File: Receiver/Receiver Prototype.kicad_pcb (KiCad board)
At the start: 4 copper layers, 145 x 50.8 mm, 96 parts, among them J1 Conn_01x02_Socket, J10 Conn_01x01, J11 Conn_Coaxial, J12 Conn_Coaxial, J13 Conn_Coaxial, J14 Conn_Coaxial, J15 Conn_01x01, J17 Conn_01x02, J18 Conn_01x02, J2 Conn_01x01, J20 Conn_01x01, J21 Conn_01x01, J22 Conn_01x01, J23 Conn_01x02, J24 Conn_01x02, J25 Conn_01x01, J26 Conn_01x03, J27 Conn_01x03, J28 Conn_01x02, J3 Conn_01x01, J4 Conn_Coaxial, J5 Conn_01x01, J6 Conn_01x02, J7 Conn_Coaxial, J8 Conn_Coaxial, J9 Conn_01x01, U1 OPA3692ID, U2 AD8692ARZ, U3 OPA692IDBVR, U4 LT3045EMSE-PBF, U5 AD607ARSZ, U6 LT3094EMSE-PBF

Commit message: DR2
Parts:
- J13, J14: footprint BNC 112404:CONN_112404_AMP -> Connector_Coaxial:BNC_Amphenol_B6252HB-NPP3G-50_Horizontal
- moved J25 8.11 mm to (187.2, 80.0)
- moved J8 6.03 mm to (179.7, 98.1)
- moved J14 5.50 mm to (196.5, 87.7), turned to 180 degrees
- moved J13 4.36 mm to (215.5, 87.7), turned to 180 degrees
- moved J7 3.50 mm to (165.2, 98.1)
- moved J15 1.58 mm to (206.8, 80.0)
- moved J2 1.50 mm to (224.2, 80.0)
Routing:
- net /PWR-: track 73.7 -> 63.1 mm
- net /PWR+: track 76.1 -> 69.1 mm
- net /I_Filter_In: track 29.3 -> 27.9 mm
- net GND: vias 10 -> 14

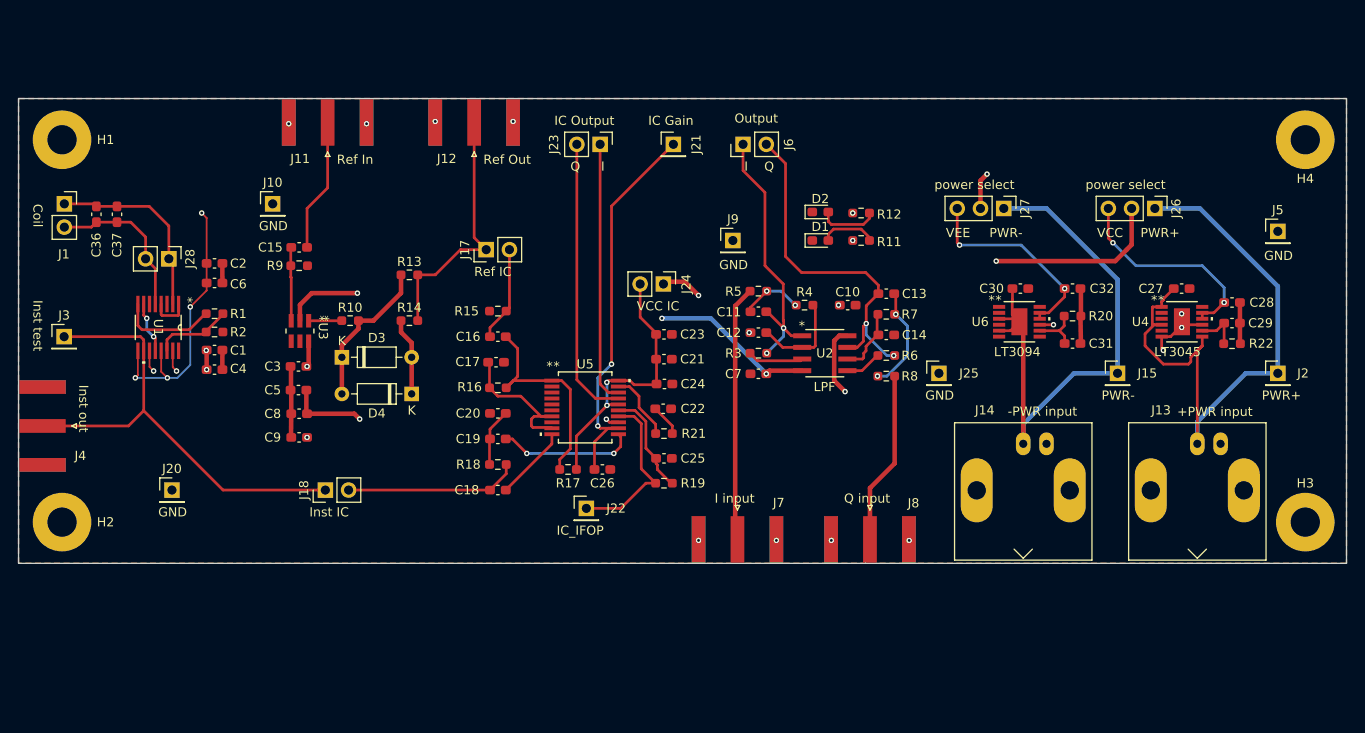
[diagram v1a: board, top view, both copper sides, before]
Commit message: Moved some components. Design not complete for the DR2
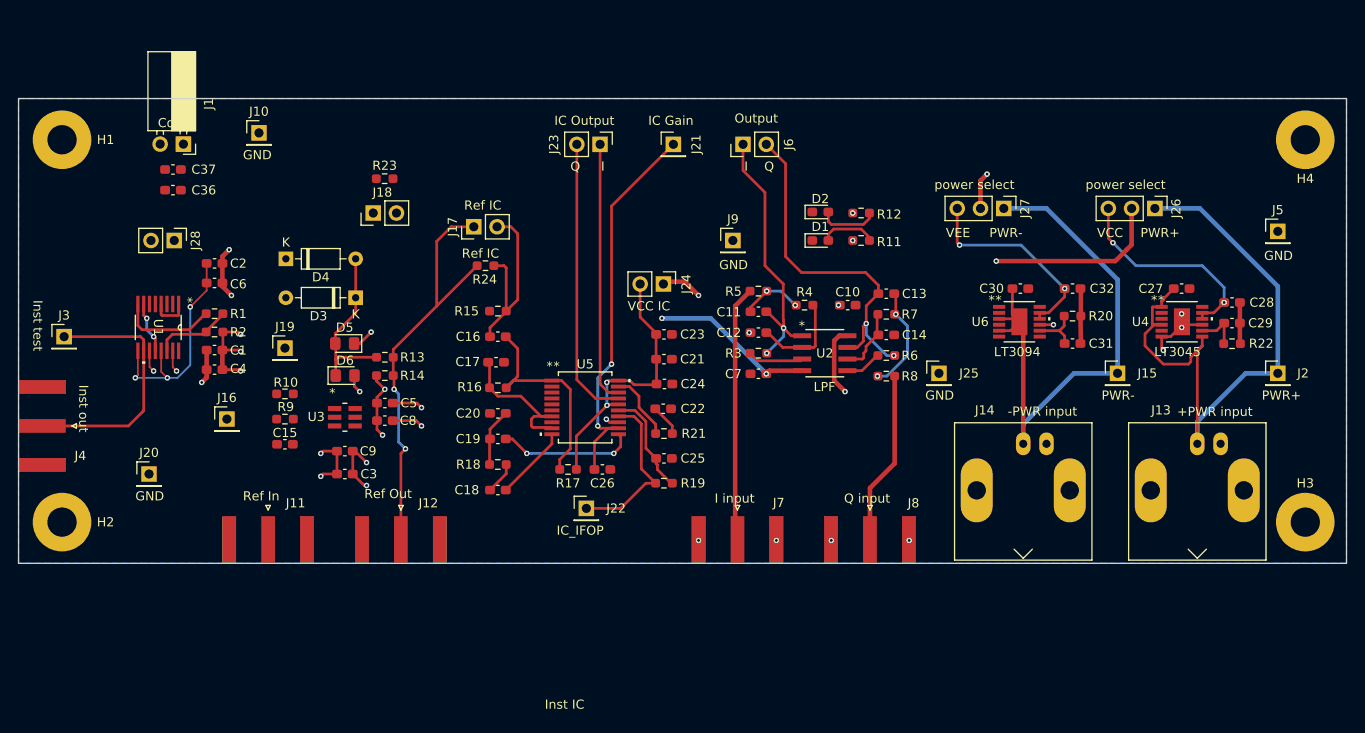
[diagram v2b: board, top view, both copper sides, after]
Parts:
- added D5: 1N4148, Diode_SMD:D_0805_2012Metric_Pad1.15x1.40mm_HandSolder, F.Cu at (122.4, 76.8)
- added D6: 1N4148, Diode_SMD:D_0805_2012Metric_Pad1.15x1.40mm_HandSolder, F.Cu at (122.4, 80.2)
- added J16: Conn_01x01, Connector_PinHeader_2.54mm:PinHeader_1x01_P2.54mm_Vertical, F.Cu at (109.5, 85.0)
- added J19: Conn_01x01, Connector_PinHeader_2.54mm:PinHeader_1x01_P2.54mm_Vertical, F.Cu at (115.8, 77.2)
- added R23: 0, Resistor_SMD:R_0603_1608Metric_Pad0.98x0.95mm_HandSolder, F.Cu at (126.7, 58.8)
- added R24: 0, Resistor_SMD:R_0603_1608Metric_Pad0.98x0.95mm_HandSolder, F.Cu at (137.7, 68.2)
- J1: footprint Connector_PinSocket_2.54mm:PinSocket_1x02_P2.54mm_Vertical -> Connector_PinSocket_2.54mm:PinSocket_1x02_P2.54mm_Horizontal
- moved J12 46.2 mm to (128.5, 98.1), turned to -90 degrees
- moved J11 46.0 mm to (114.0, 98.1), turned to -90 degrees
- moved J18 30.7 mm to (125.5, 62.5)
- moved C15 21.6 mm to (115.8, 87.8), turned to 0 degrees
- moved D4 20.2 mm to (115.9, 67.5), turned to 0 degrees
- moved R9 16.8 mm to (115.8, 85.0), turned to 180 degrees
- moved J1 14.5 mm to (104.8, 55.0), turned to -90 degrees
- moved C3 12.8 mm to (122.4, 91.0)
- moved R10 10.7 mm to (115.8, 82.2)
- moved U3 10.6 mm to (122.4, 84.8), turned to 0 degrees
- moved C5 9.54 mm to (126.8, 83.2)
- moved C8 9.39 mm to (126.8, 85.2)
- moved R13 9.39 mm to (126.8, 78.2)
- moved C36 8.77 mm to (103.6, 60.0), turned to 0 degrees
- moved J10 7.89 mm to (113.0, 53.8)
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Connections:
- net Net-(U3-IN+) renamed /Buff_In
- net Net-(U3-OUPUT) renamed /Buff_Out
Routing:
- net /Inst_Out: track 70.7 -> 31.8 mm
- net /Reference_Out: track 38.4 -> 67.5 mm, vias 0 -> 2
- net /INA: track 21.1 -> 0.00 mm
- net /INB: track 17.5 -> 0.00 mm
- net VEE: track 69.7 -> 53.5 mm, vias 10 -> 9
- net /Reference_In: track 14.6 -> 0.00 mm
- net GND: track 42.3 -> 55.9 mm, vias 14 -> 21
- net /Buff_In: track 8.06 -> 0.00 mm
- net VCC: track 41.6 -> 46.9 mm, vias 11 -> 10
- net /Buff_Out: track 3.62 -> 0.00 mm
- net Net-(D3-K): track 16.6 -> 18.3 mm
- removed copper zone on F.Cu, net GND

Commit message: Receiver ready for design review 2
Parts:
- moved J18 36.3 mm to (103.0, 91.0)
- moved R23 35.5 mm to (104.2, 86.2)
- moved J1 25.3 mm to (129.8, 51.4)
- moved C37 25.0 mm to (128.5, 55.4), turned to 180 degrees
- moved C36 24.9 mm to (128.5, 58.4), turned to 180 degrees
- moved J10 11.8 mm to (102.0, 58.1)
- moved J28 9.12 mm to (112.5, 62.8), turned to 180 degrees
- moved J20 3.75 mm to (97.2, 91.0)
- moved R24 1.84 mm to (139.1, 69.5)
- moved J17 1.78 mm to (137.7, 65.2)
- moved J16 1.77 mm to (110.8, 83.8)
- moved J19 1.76 mm to (116.8, 75.8)
- moved J15 1.75 mm to (205.0, 80.0)
- moved J25 1.75 mm to (189.0, 80.0)
- moved U3 1.75 mm to (122.4, 86.5)
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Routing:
- net /Inst_Out: track 31.8 -> 82.6 mm, vias 0 -> 2
- net /INA: track 0.00 -> 43.6 mm
- net /INB: track 0.00 -> 43.3 mm
- net GND: track 55.9 -> 39.1 mm, vias 21 -> 218
- net /Buff_Out: track 0.00 -> 15.9 mm
- net /Buff_In: track 0.00 -> 12.8 mm
- net /Reference_In: track 0.00 -> 10.8 mm
- net /Reference_Out: track 67.5 -> 58.8 mm
- net VEE: track 53.5 -> 62.2 mm, vias 9 -> 11
- net Net-(D3-K): track 18.3 -> 23.7 mm
- net /PWR+: track 69.1 -> 63.7 mm
- net /PWR-: track 63.1 -> 59.5 mm
- net Net-(C13-Pad2): track 11.5 -> 13.8 mm
- net Net-(U5-GREF): track 16.4 -> 15.2 mm
- net /I_Filter_Out: track 30.4 -> 31.3 mm
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- added copper zone on F.Cu, net GND
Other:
- outline, holes or cut-outs redrawn
- board text added: "Buff In"
- board text added: "Buff Out"
- board text added: "Coil test"

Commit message: Receiver minor fixes before DR2
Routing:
- net VEE: track 62.2 -> 52.6 mm, vias 11 -> 12
- net /IC_Gain: track 42.8 -> 45.5 mm
- net /VCC_IC: track 29.8 -> 31.9 mm
- net /IC_I: track 28.6 -> 30.2 mm
- net GND: track 39.1 -> 38.7 mm, vias 218 -> 224

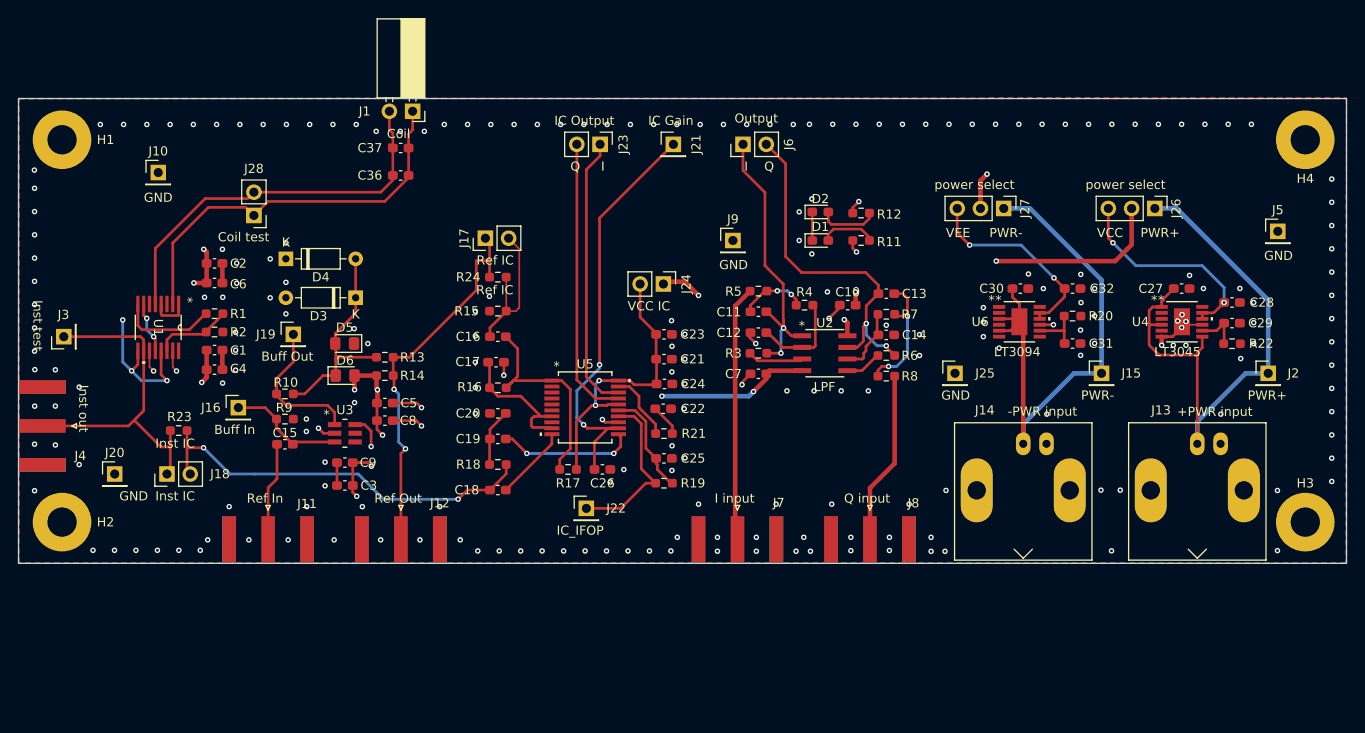
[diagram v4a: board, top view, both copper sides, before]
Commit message: Added filter input select for In-phase
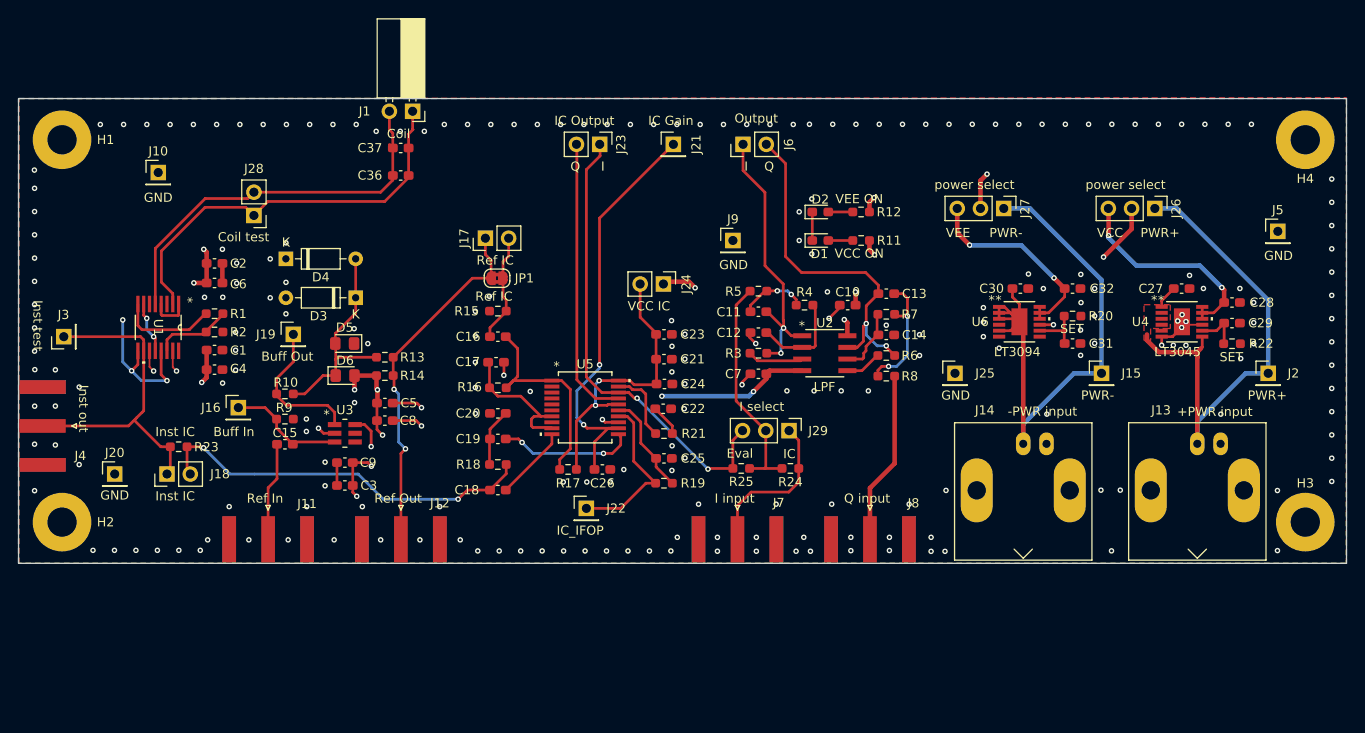
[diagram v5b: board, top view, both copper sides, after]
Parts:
- added J29: Conn_01x03, Connector_PinHeader_2.54mm:PinHeader_1x03_P2.54mm_Vertical, F.Cu at (170.9, 86.3)
- added JP1: Jumper_2_Bridged, Jumper:SolderJumper-2_P1.3mm_Bridged2Bar_RoundedPad1.0x1.5mm, F.Cu at (139.0, 69.6)
- added R25: 0, Resistor_SMD:R_0603_1608Metric_Pad0.98x0.95mm_HandSolder, F.Cu at (165.7, 90.4)
- moved R24 38.2 mm to (171.0, 90.4), turned to 180 degrees
- moved R23 1.77 mm to (104.2, 88.0)
- moved R12 0.12 mm to (178.8, 62.4), turned to 180 degrees
- turned R11 to 180 degrees
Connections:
- net /IC_I renamed /I_Filter_In_IC
- J7 pad 1: /I_Filter_In -> /I_Filter_In_Eval
- R24 pad 1: /Reference_Out -> /I_Filter_In_Eval
- R24 pad 2: /Reference_Out -> /I_Filter_In
- U4 pad 12: unconnected-(U4-OUT-Pad12) -> /VCC_In
- U4 pad 2: unconnected-(U4-IN-Pad2) -> /PWR+
- U4 pad 3: unconnected-(U4-IN-Pad3) -> /PWR+
- U6 pad 1: unconnected-(U6-IN-Pad1) -> /PWR-
- U6 pad 12: unconnected-(U6-OUT-Pad12) -> /VEE_In
- U6 pad 2: unconnected-(U6-IN-Pad2) -> /PWR-
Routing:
- net /I_Filter_In_IC: track 30.2 -> 50.8 mm, vias 0 -> 2
- net /I_Filter_In_Eval: track 0.00 -> 17.5 mm
- net VCC: track 47.7 -> 34.5 mm
- net /Reference_Out: track 58.8 -> 51.4 mm
- net /PWR-: track 59.5 -> 66.3 mm
- net /PWR+: track 63.7 -> 58.0 mm
- net Net-(D2-A): track 6.53 -> 2.72 mm
- net /Inst_Out: track 82.6 -> 79.1 mm
- net Net-(D1-A): track 6.12 -> 2.67 mm
- net /I_Filter_In: track 27.9 -> 24.9 mm
- net GND: track 38.7 -> 36.5 mm, vias 224 -> 227
- net /INA: track 43.6 -> 44.8 mm
- net /VEE_In: track 21.9 -> 22.6 mm
- net Net-(U5-FLTR): track 7.52 -> 8.06 mm
- added copper zone on F.Cu, net /PWR+
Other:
- board text added: "Eval"
- board text added: "I select"
- board text added: "IC"
- board text added: "SET"
- board text added: "VCC ON"
- board text added: "VEE ON"

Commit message: Added new diodes and 3d models for BNC
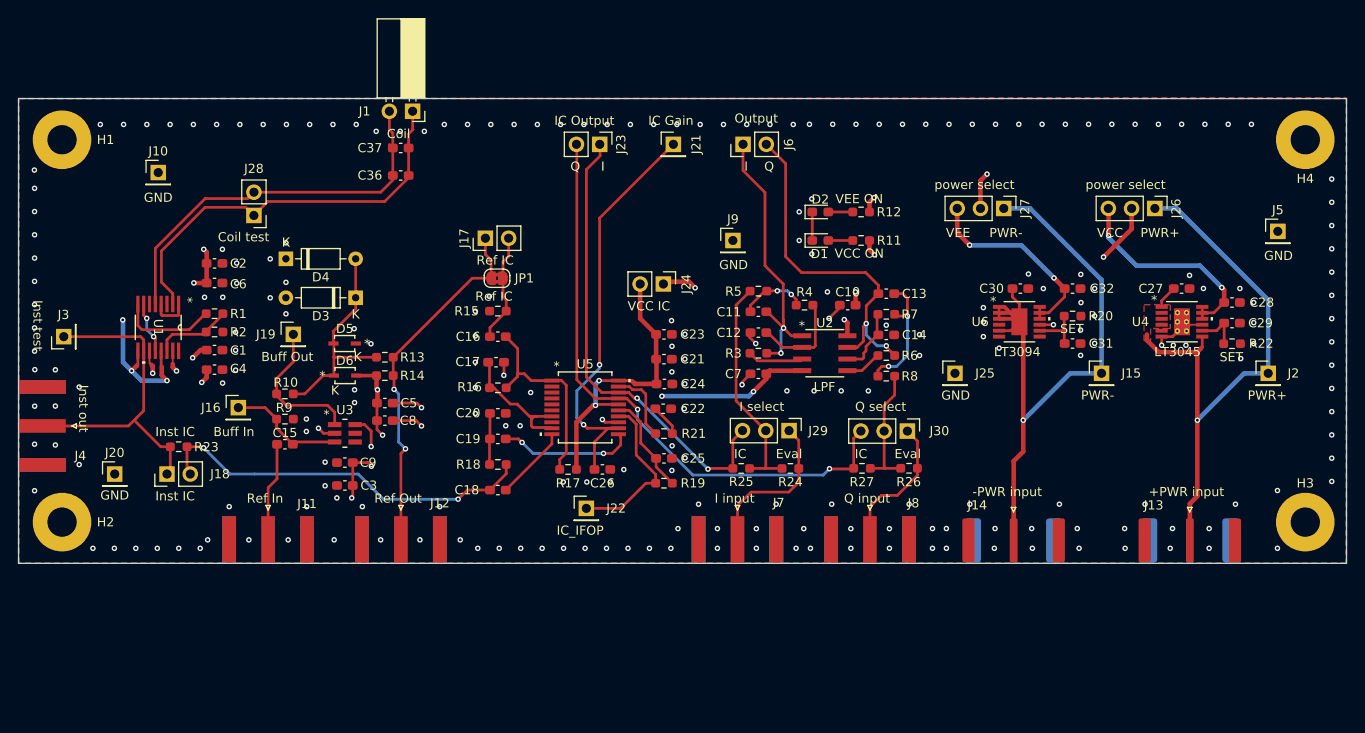
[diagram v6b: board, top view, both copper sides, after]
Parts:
- added J30: Conn_01x03, Connector_PinHeader_2.54mm:PinHeader_1x03_P2.54mm_Vertical, F.Cu at (183.8, 86.3)
- added R26: 0, Resistor_SMD:R_0603_1608Metric_Pad0.98x0.95mm_HandSolder, F.Cu at (184.0, 90.4)
- added R27: 0, Resistor_SMD:R_0603_1608Metric_Pad0.98x0.95mm_HandSolder, F.Cu at (178.8, 90.4)
- D5, D6: footprint Diode_SMD:D_0805_2012Metric_Pad1.15x1.40mm_HandSolder -> 1N4148WS-HE3-18:CR_HE3-18_VIS
- J13, J14: footprint Connector_Coaxial:BNC_Amphenol_B6252HB-NPP3G-50_Horizontal -> BNC 112640:BNC_Amphenol_112640_Edge_mount
- R11, R12: value 4.7k -> 400
- moved J14 8.24 mm to (195.4, 95.9), turned to -90 degrees
- moved J13 8.22 mm to (214.7, 95.9), turned to -90 degrees
- turned C20 to 0 degrees
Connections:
- net /IC_Q renamed /Q_Filter_In_IC
- J8 pad 1: /Q_Filter_In -> /Q_Filter_In_Eval
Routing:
- net /Q_Filter_In_IC: track 31.1 -> 65.6 mm, vias 0 -> 2
- net /Q_Filter_In_Eval: track 0.00 -> 15.4 mm
- net /PWR-: track 66.3 -> 75.0 mm, vias 0 -> 1
- net /PWR+: track 58.0 -> 66.4 mm, vias 0 -> 1
- net GND: track 36.5 -> 30.3 mm, vias 227 -> 237
- net /Q_Filter_In: track 18.9 -> 13.9 mm
- net Net-(U5-FDIN): track 23.6 -> 22.0 mm
- net Net-(C19-Pad2): track 6.32 -> 5.60 mm
- net VCC: track 34.5 -> 34.6 mm, vias 11 -> 12
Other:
- board text added: "*"
- board text added: "K"
- board text added: "Q select"

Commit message: Changed the AD8692 and SMD diodes footprints
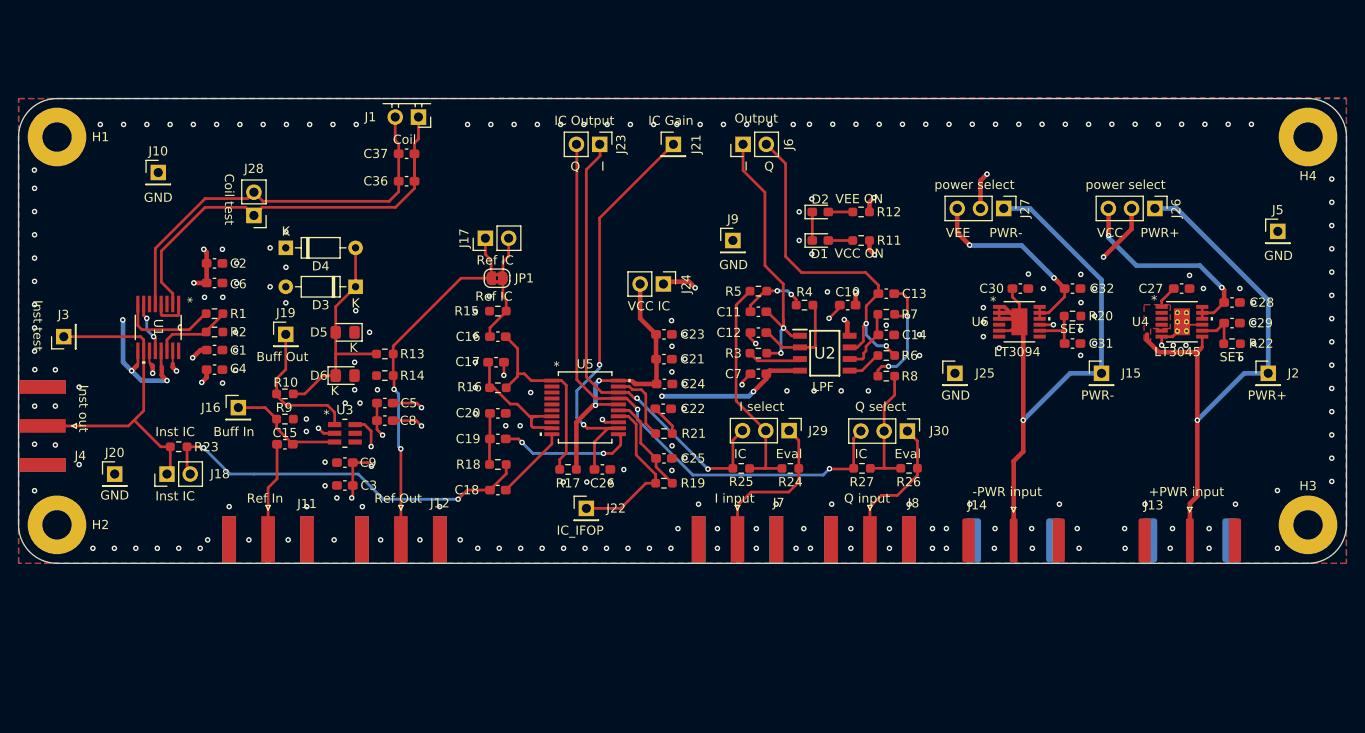
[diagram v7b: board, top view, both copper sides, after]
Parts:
- D5, D6: footprint 1N4148WS-HE3-18:CR_HE3-18_VIS -> Diode_SMD:D_0805_2012Metric_Pad1.15x1.40mm_HandSolder
- U2: footprint AD8692:R-8_ADI -> AD8692:SOIC127P600X175-8N
- moved D5 1.22 mm to (122.4, 75.5)
- moved D3 1.20 mm to (123.5, 70.5)
- moved D4 1.20 mm to (115.9, 66.3)
- moved C36 0.90 mm to (129.1, 59.0)
- moved C37 0.90 mm to (129.1, 56.0)
- moved J1 0.90 mm to (130.4, 52.0)
- moved J19 0.82 mm to (115.9, 75.8)
- moved H1 0.63 mm to (91.0, 54.2)
- moved H2 0.63 mm to (91.0, 96.5)
- moved H3 0.42 mm to (227.6, 96.5)
- moved H4 0.42 mm to (227.6, 54.2)
- moved R13 0.36 mm to (126.8, 77.9)
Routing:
- net GND: track 30.3 -> 25.1 mm, vias 237 -> 235
- net /INA: track 44.8 -> 48.5 mm
- net Net-(D3-K): track 23.7 -> 24.8 mm
- net /INB: track 43.3 -> 44.3 mm
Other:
- outline, holes or cut-outs redrawn
- board text added: "Receiver 1.0 2024-05-02"
- board text removed: "Receiver 1.0 2024-04-01"
